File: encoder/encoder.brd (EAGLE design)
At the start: 17.8 x 27.6 mm, 17 parts, among them SW1 EC12E_SW, U1 SN74LVC1G14DBVRDBV5-L, U2 SN74LVC1G14DBVRDBV5-L, U3 SN74LVC1G14DBVRDBV5-L

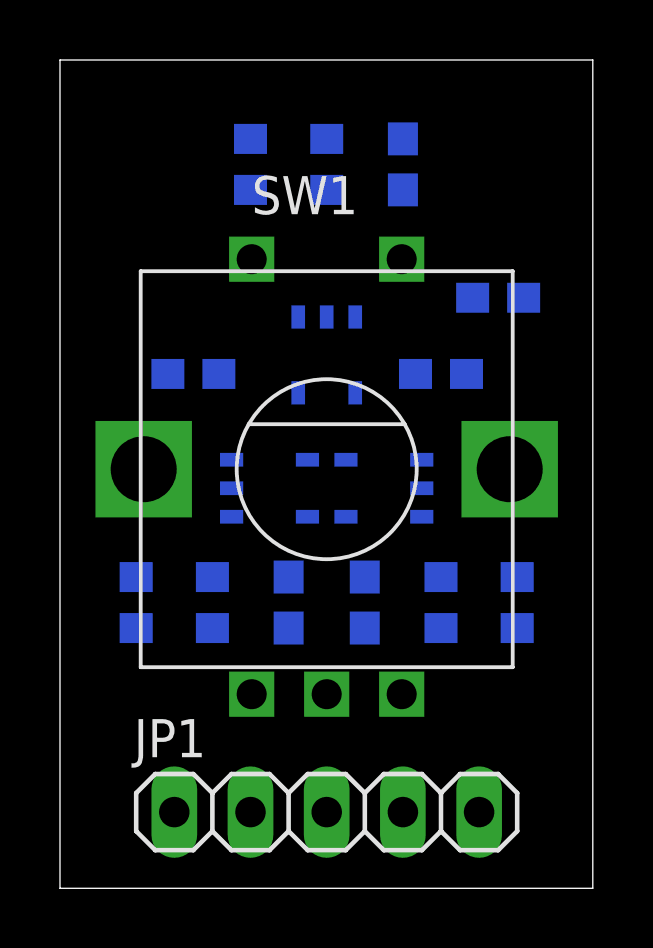
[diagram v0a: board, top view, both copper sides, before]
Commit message: Added SD breakout
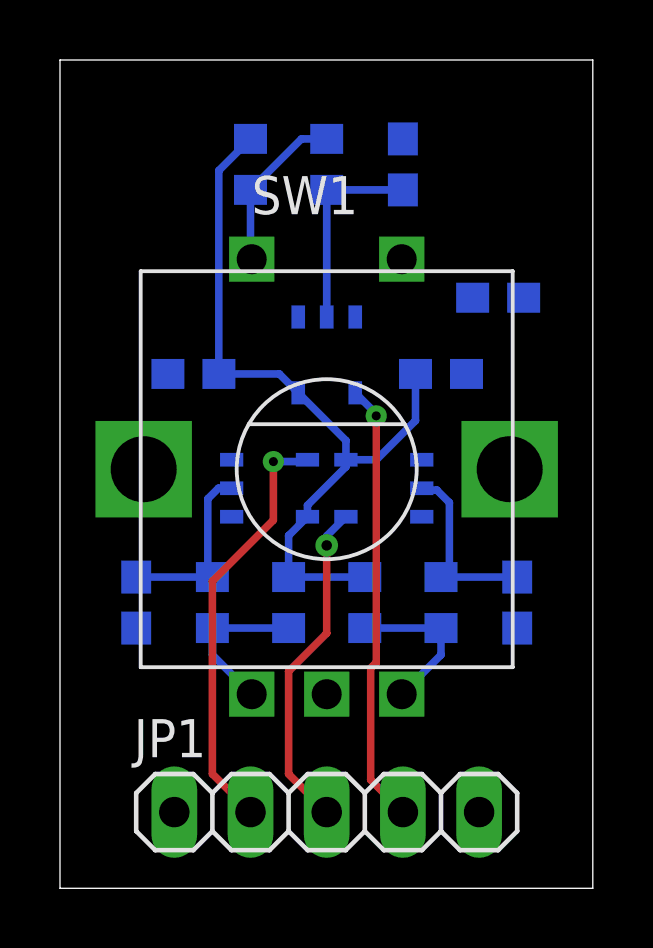
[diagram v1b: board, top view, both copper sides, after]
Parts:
- moved C2 5.08 mm to (15.2, 9.53)
- moved C3 5.08 mm to (2.54, 9.53)
- moved R5 5.08 mm to (10.2, 9.53)
- moved R6 5.08 mm to (7.62, 9.53)
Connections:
- net A: now also JP1.2; no longer JP1.3
- net B: now also JP1.3; no longer JP1.2
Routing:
- net 3.3V: track 0.00 -> 25.7 mm
- net SW: track 0.00 -> 14.8 mm, vias 0 -> 1
- net A: track 0.00 -> 14.2 mm, vias 0 -> 1
- net B: track 0.00 -> 11.2 mm, vias 0 -> 1
- net SW_RC: track 0.00 -> 6.78 mm
- net B_RC: track 0.00 -> 6.26 mm
- net A_RC: track 0.00 -> 6.15 mm
- net N$1: track 0.00 -> 5.57 mm
- net N$3: track 0.00 -> 5.46 mm
- net N$4: track 0.00 -> 5.29 mm
